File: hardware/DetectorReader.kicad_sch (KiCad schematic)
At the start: 22 parts, among them J1 Combo_Conn, J2 CON-SMA-EDGE-S, J3 USB_C_Receptacle_USB2.0_16P, U1 XC0900P-10S, U2 ATtiny814-SS, U3 TLV70330DBVR, U4 CY7C65211-24LTXI

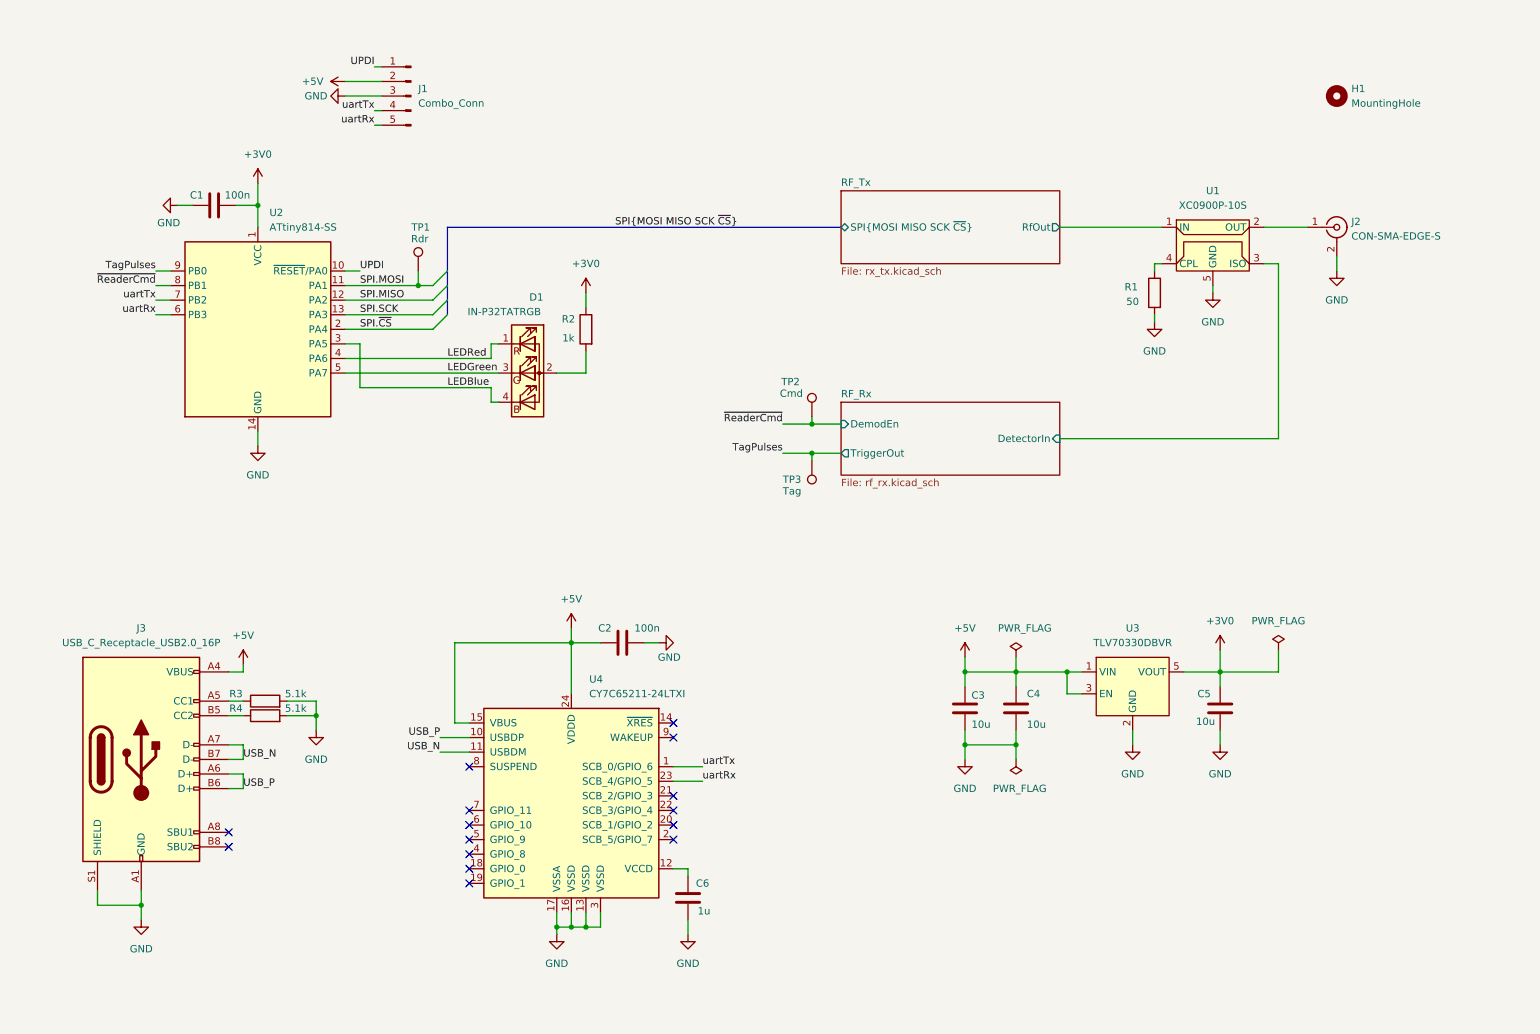
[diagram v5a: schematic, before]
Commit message: Rev 4. Removed coupler and detector IC. Using simple diode as detector.
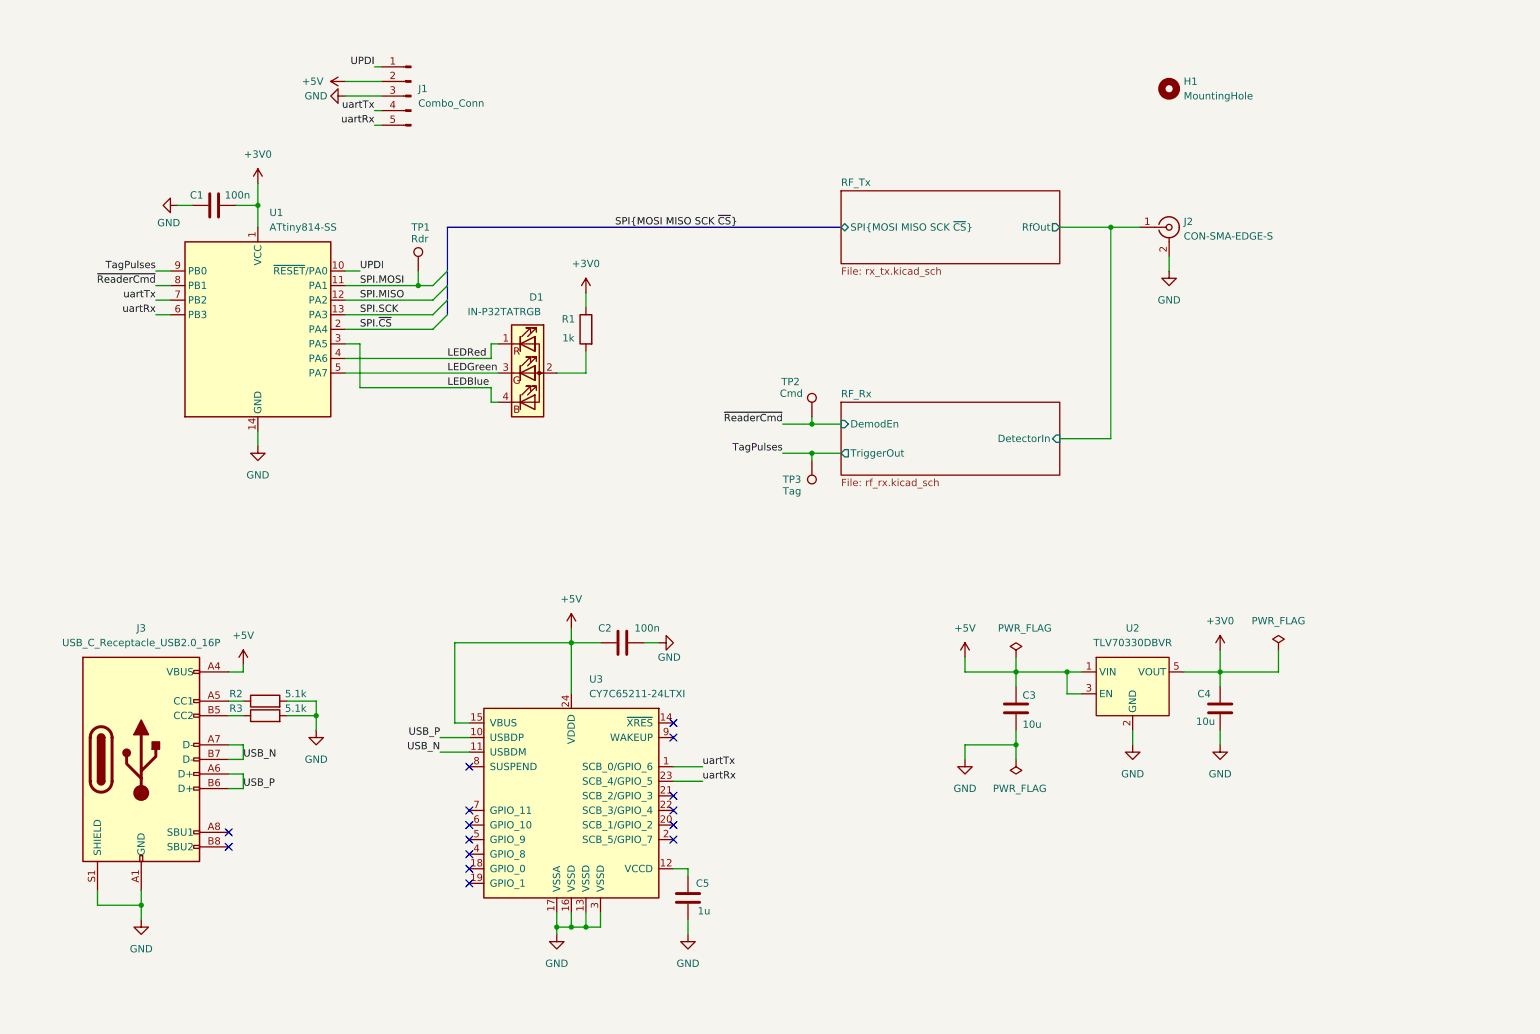
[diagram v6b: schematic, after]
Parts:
- removed C4: 10u, Capacitor_SMD:C_0603_1608Metric, symbol Device:C
- removed R1: 50, Resistor_SMD:R_0603_1608Metric, symbol Device:R
- removed U1: XC0900P-10S, ProjLib:Xinger2, symbol ProjLib:XC0900P-10S
- renumbered C5 to C4, C6 to C5, R2 to R1, R3 to R2, R4 to R3, U2 to U1, U3 to U2, U4 to U3
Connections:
- net RF_Rx/DetectorIn: now also J2.1 (In)
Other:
- moved on the sheet: C3, H1, J2

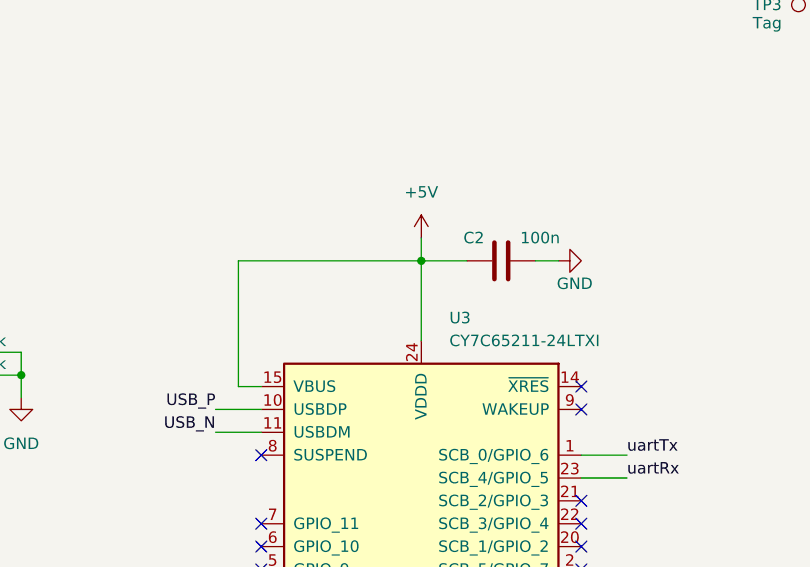
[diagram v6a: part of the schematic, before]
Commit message: Fixed UART bridge power supply. Made board 1 mm shorter.
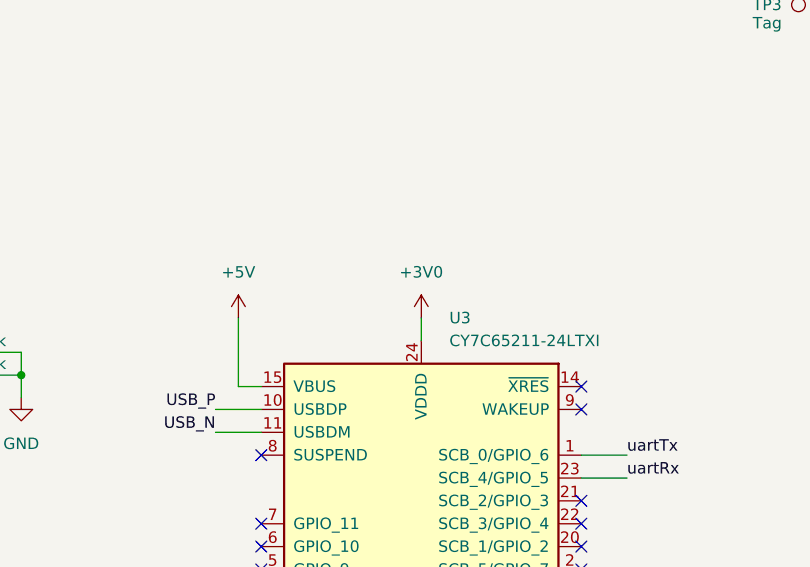
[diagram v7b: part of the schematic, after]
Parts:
- removed C2: 100n, Capacitor_SMD:C_0603_1608Metric, symbol Device:C
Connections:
- net +3V0: now also U3.24 (VDDD)
- net +5V: no longer U3.24 (VDDD)
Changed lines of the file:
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@@
 	)
 	(junction
-		(at 111.76 123.19)
-		(diameter 0)
-		(color 0 0 0 0)
-	)
-	(junction
 		(at 109.22 172.72)
 		(diameter 0)
@@
 	(wire
 		(pts
-			(xy 127 123.19) (xy 124.46 123.19)
-		)
-		(stroke
-			(width 0)
-			(type default)
-		)
-	)
-	(wire
-		(pts
 			(xy 109.22 170.18) (xy 109.22 172.72)
 		)
@@
 	(wire
 		(pts
-			(xy 111.76 123.19) (xy 116.84 123.19)
-		)
-		(stroke
-			(width 0)
-			(type default)
-		)
-	)
-	(wire
-		(pts
 			(xy 189.23 143.51) (xy 189.23 140.97)
 		)
@@
 	(wire
 		(pts
-			(xy 111.76 120.65) (xy 111.76 123.19)
+			(xy 111.76 129.54) (xy 111.76 132.08)
 		)
 		(stroke
@@
 	(wire
 		(pts
-			(xy 111.76 123.19) (xy 111.76 132.08)
-		)
-		(stroke
-			(width 0)
-			(type default)
-		)
-	)
-	(wire
-		(pts
-			(xy 91.44 137.16) (xy 91.44 123.19)
+			(xy 91.44 137.16) (xy 91.44 129.54)
 		)
 		(stroke
@@
 	(wire
 		(pts
-			(xy 91.44 123.19) (xy 111.76 123.19)
-		)
-		(stroke
-			(width 0)
-			(type default)
-		)
-	)
-	(wire
-		(pts
 			(xy 72.39 66.04) (xy 87.63 66.04)
 		)
@@
 	)
 	(symbol
+		(lib_id "power:+3V0")
+		(at 111.76 129.54 0)
+		(unit 1)
+		(exclude_from_sim no)
+		(in_bom yes)
+		(on_board yes)
+		(dnp no)
+		(fields_autoplaced yes)
+		(property "Reference" "#PWR039"
+			(at 111.76 133.35 0)
+			(effects
+				(font
+					(size 1.27 1.27)
+				)
+				(hide yes)
+			)
+		)
+		(property "Value" "+3V0"
+			(at 111.76 124.46 0)
+			(effects
+				(font
+					(size 1.27 1.27)
+				)
+			)
+		)
+		(property "Footprint" ""
+			(at 111.76 129.54 0)
+			(effects
+				(font
+					(size 1.27 1.27)
+				)
+				(hide yes)
+			)
+		)
+		(property "Datasheet" ""
+			(at 111.76 129.54 0)
+			(effects
+				(font
+					(size 1.27 1.27)
+				)
+				(hide yes)
+			)
+		)
+		(property "Description" ""
+			(at 111.76 129.54 0)
+			(effects
+				(font
+					(size 1.27 1.27)
+				)
+			)
+		)
+		(pin "1"
+		)
+		(instances
+			(project "DetectorReader"
+				(path "/e63e39d7-6ac0-4ffd-8aa3-1841a4541b55"
+					(reference "#PWR039")
+					(unit 1)
+				)
+			)
+		)
+	)
+	(symbol
 		(lib_id "power:+5V")
 		(at 180.34 125.73 0)
@@
 	(symbol
 		(lib_id "power:GND")
-		(at 127 123.19 90)
-		(mirror x)
-		(unit 1)
-		(exclude_from_sim no)
-		(in_bom yes)
-		(on_board yes)
-		(dnp no)
-		(property "Reference" "#PWR09"
-			(at 133.35 123.19 0)
-			(effects
-				(font
-					(size 1.27 1.27)
-				)
-				(hide yes)
-			)
-		)
-		(property "Value" "GND"
-			(at 130.81 125.73 90)
-			(effects
-				(font
-					(size 1.27 1.27)
-				)
-				(justify left)
-			)
-		)
-		(property "Footprint" ""
-			(at 127 123.19 0)
-			(effects
-				(font
-					(size 1.27 1.27)
-				)
-				(hide yes)
-			)
-		)
-		(property "Datasheet" ""
-			(at 127 123.19 0)
-			(effects
-				(font
-					(size 1.27 1.27)
-				)
-				(hide yes)
-			)
-		)
-		(property "Description" ""
-			(at 127 123.19 0)
-			(effects
-				(font
-					(size 1.27 1.27)
-				)
-			)
-		)
-		(pin "1"
-		)
-		(instances
-			(project "DetectorReader"
-				(path "/e63e39d7-6ac0-4ffd-8aa3-1841a4541b55"
-					(reference "#PWR09")
-					(unit 1)
-				)
-			)
-		)
-	)
-	(symbol
-		(lib_id "power:GND")
 		(at 109.22 173.99 0)
 		(unit 1)
@@
 	)
 	(symbol
-		(lib_id "Device:C")
-		(at 120.65 123.19 270)
-		(mirror x)
-		(unit 1)
-		(exclude_from_sim no)
-		(in_bom yes)
-		(on_board yes)
-		(dnp no)
-		(property "Reference" "C2"
-			(at 117.602 120.65 90)
-			(effects
-				(font
-					(size 1.27 1.27)
-				)
-			)
-		)
-		(property "Value" "100n"
-			(at 124.968 120.65 90)
-			(effects
-				(font
-					(size 1.27 1.27)
-				)
-			)
-		)
-		(property "Footprint" "Capacitor_SMD:C_0603_1608Metric"
-			(at 116.84 122.2248 0)
-			(effects
-				(font
-					(size 1.27 1.27)
-				)
-				(hide yes)
-			)
-		)
-		(property "Datasheet" "~"
-			(at 120.65 123.19 0)
-			(effects
-				(font
-					(size 1.27 1.27)
-				)
-				(hide yes)
-			)
-		)
-		(property "Description" ""
-			(at 120.65 123.19 0)
-			(effects
-				(font
-					(size 1.27 1.27)
-				)
-			)
-		)
-		(pin "1"
-		)
-		(pin "2"
-		)
-		(instances
-			(project "DetectorReader"
-				(path "/e63e39d7-6ac0-4ffd-8aa3-1841a4541b55"
-					(reference "C2")
-					(unit 1)
-				)
-			)
-		)
-	)
-	(symbol
 		(lib_id "power:GND")
 		(at 215.9 58.42 0)
@@
 	(symbol
 		(lib_id "power:+5V")
-		(at 111.76 120.65 0)
+		(at 91.44 129.54 0)
 		(mirror y)
 		(unit 1)
@@
 		(fields_autoplaced yes)
 		(property "Reference" "#PWR08"
-			(at 111.76 124.46 0)
+			(at 91.44 133.35 0)
 			(effects
 				(font
@@
 		)
 		(property "Value" "+5V"
-			(at 111.76 115.57 0)
+			(at 91.44 124.46 0)
 			(effects
 				(font
@@
 		)
 		(property "Footprint" ""
-			(at 111.76 120.65 0)
+			(at 91.44 129.54 0)
 			(effects
 				(font
@@
 		)
 		(property "Datasheet" ""
-			(at 111.76 120.65 0)
+			(at 91.44 129.54 0)
 			(effects
 				(font
@@
 		)
 		(property "Description" ""
-			(at 111.76 120.65 0)
+			(at 91.44 129.54 0)
 			(effects
 				(font

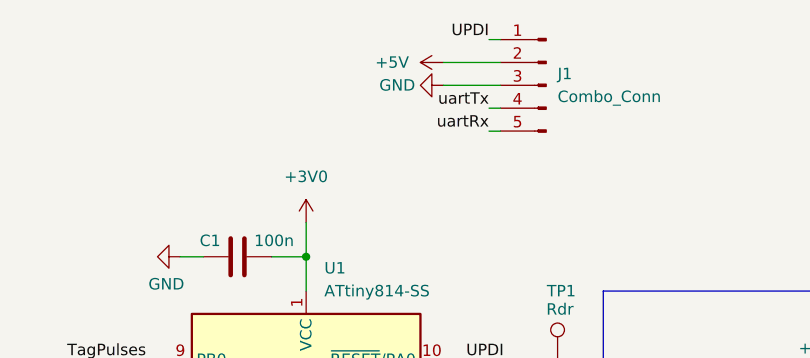
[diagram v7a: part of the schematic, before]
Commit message: Fixed connector pinout according to silkscreen
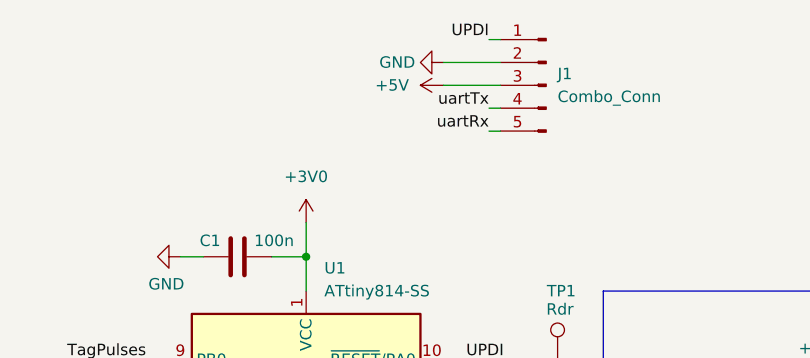
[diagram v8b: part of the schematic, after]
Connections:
- net +5V: now also J1.3 (Pin_3); no longer J1.2 (Pin_2)
- net GND: now also J1.2 (Pin_2); no longer J1.3 (Pin_3)
